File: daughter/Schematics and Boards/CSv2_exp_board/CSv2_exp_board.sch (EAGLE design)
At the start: 139 parts, among them J1 HIROSE-DF40_44-PIN_CONNECTORS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, J2 J-SERIAL-PORT, J3 CORTEX_DEBUG_SMD, J301 HIROSE-DF40_44-PIN_CONNECTORS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, J4 SJ-43514-SMT, J7 J-USB-HIROSE-MICRO-USB, SW1 SPST_TACT-KMR2, SW2 SPST_TACT-KMR2, U1 LOADSWITCH-MIC94164, U10 LOADSWITCH-MIC94164, U11 BMI160, U12 TLV320DAC26IRHB, U13 ADG839YKSZ-500RL7KS_6_ADI-L, U14 LOADSWITCH-MIC94164, U15 LP2980AIM5-2.5/NOPBMF05A_TEX-L, U16 NCP553SQ18T1GSC-82AB_ONS-L, U2 ADA4841-1YRJZ-R7, U205 MPL3115A2, U3 Value, U4 RFM69HCW, U5 Value, U6 Value, U7 LOADSWITCH-MIC94164, U8 LOADSWITCH-MIC94164, U9 LOADSWITCH-MIC94164, X1 32.768kHz, X2 32.768, X3 uFL, X4 uFL, X5 uFL, X6 uFL

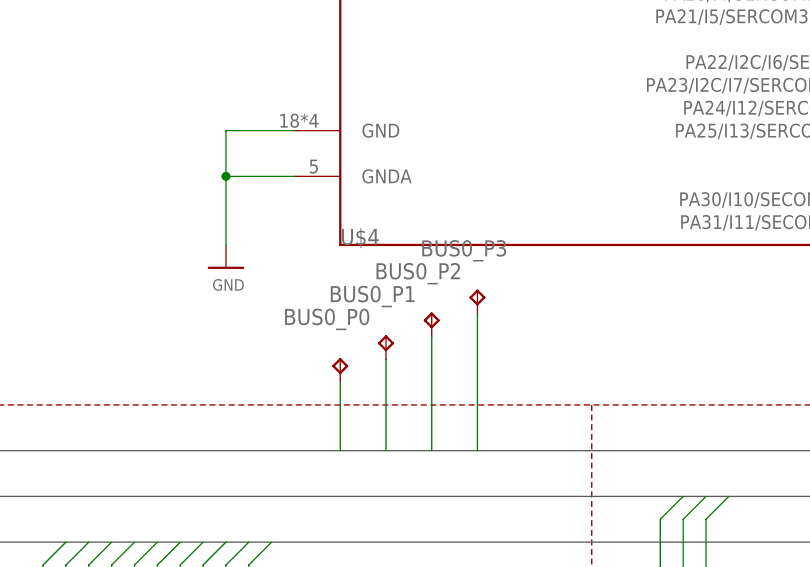
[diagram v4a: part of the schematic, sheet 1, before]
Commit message: DTR-drc resolved, schematic check, routing  check
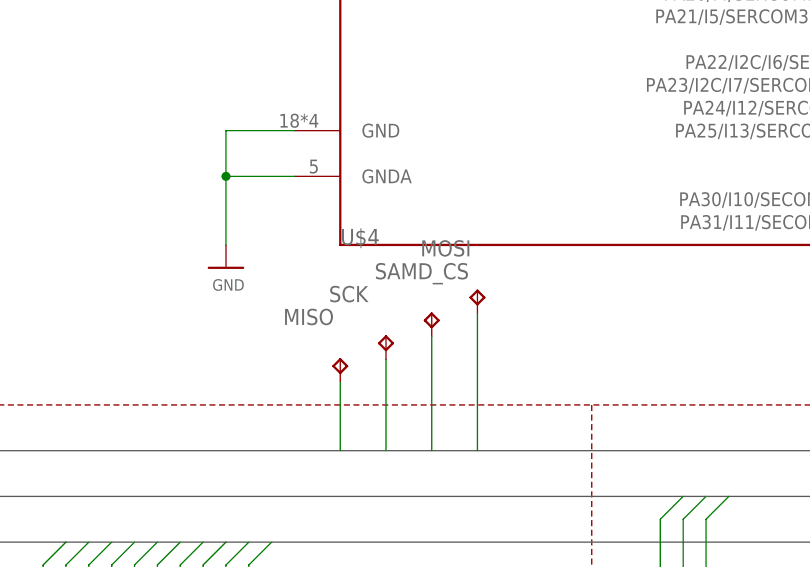
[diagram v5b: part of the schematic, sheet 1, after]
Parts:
- added CODEC_CS: TPTP10SQ, TestPoints:TPTP10SQ
- renumbered BUS0_P0 to MISO, BUS0_P1 to SCK, BUS0_P2 to SAMD_CS, BUS0_P3 to MOSI
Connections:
- net BUS0_GPIO1: now also CODEC_CS.TP
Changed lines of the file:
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@@
 <part name="BUS1_SDA" library="TestPoints" deviceset="TP" device="TP10SQ" package3d_urn="urn:adsk.eagle:package:27962/1" value="TPTP10SQ"/>
 <part name="USB_V" library="TestPoints" deviceset="TP" device="TP10SQ" package3d_urn="urn:adsk.eagle:package:27962/1" value="TPTP10SQ"/>
-<part name="BUS0_P0" library="TestPoints" deviceset="TP" device="TP10SQ" package3d_urn="urn:adsk.eagle:package:27962/1" value="TPTP10SQ"/>
-<part name="BUS0_P1" library="TestPoints" deviceset="TP" device="TP10SQ" package3d_urn="urn:adsk.eagle:package:27962/1" value="TPTP10SQ"/>
-<part name="BUS0_P2" library="TestPoints" deviceset="TP" device="TP10SQ" package3d_urn="urn:adsk.eagle:package:27962/1" value="TPTP10SQ"/>
-<part name="BUS0_P3" library="TestPoints" deviceset="TP" device="TP10SQ" package3d_urn="urn:adsk.eagle:package:27962/1" value="TPTP10SQ"/>
+<part name="MISO" library="TestPoints" deviceset="TP" device="TP10SQ" package3d_urn="urn:adsk.eagle:package:27962/1" value="TPTP10SQ"/>
+<part name="SCK" library="TestPoints" deviceset="TP" device="TP10SQ" package3d_urn="urn:adsk.eagle:package:27962/1" value="TPTP10SQ"/>
+<part name="SAMD_CS" library="TestPoints" deviceset="TP" device="TP10SQ" package3d_urn="urn:adsk.eagle:package:27962/1" value="TPTP10SQ"/>
+<part name="MOSI" library="TestPoints" deviceset="TP" device="TP10SQ" package3d_urn="urn:adsk.eagle:package:27962/1" value="TPTP10SQ"/>
 <part name="J2" library="Connectors" deviceset="J-SERIAL-PORT" device=""/>
 <part name="A1" library="CommonSense-DTR-v1" deviceset="ILA09_CHIP_ANTENNA" device=""/>
@@
 <part name="EN_MEAS" library="TestPoints" deviceset="TP" device="TP10SQ" package3d_urn="urn:adsk.eagle:package:27962/1"/>
 <part name="JP4" library="Connectors" deviceset="JUMPER-SMT_2_NC_PASTE" device="_NO-SILK" package3d_urn="urn:adsk.eagle:package:39283/1" technology="LG" value="JUMPER-SMT_2_NC_PASTELG_NO-SILK"/>
+<part name="CODEC_CS" library="TestPoints" deviceset="TP" device="TP10SQ" package3d_urn="urn:adsk.eagle:package:27962/1" value="TPTP10SQ"/>
 </parts>
 <sheets>
@@
 <attribute name="TP_SIGNAL_NAME" x="344.17" y="199.39" size="1.778" layer="97"/>
 </instance>
-<instance part="BUS0_P0" gate="G$1" x="205.74" y="132.08" smashed="yes">
+<instance part="MISO" gate="G$1" x="205.74" y="132.08" smashed="yes">
 <attribute name="NAME" x="199.39" y="135.89" size="1.778" layer="95"/>
 <attribute name="TP_SIGNAL_NAME" x="207.01" y="130.81" size="1.778" layer="97"/>
 </instance>
-<instance part="BUS0_P1" gate="G$1" x="210.82" y="134.62" smashed="yes">
+<instance part="SCK" gate="G$1" x="210.82" y="134.62" smashed="yes">
 <attribute name="NAME" x="204.47" y="138.43" size="1.778" layer="95"/>
 <attribute name="TP_SIGNAL_NAME" x="212.09" y="133.35" size="1.778" layer="97"/>
 </instance>
-<instance part="BUS0_P2" gate="G$1" x="215.9" y="137.16" smashed="yes">
+<instance part="SAMD_CS" gate="G$1" x="215.9" y="137.16" smashed="yes">
 <attribute name="NAME" x="209.55" y="140.97" size="1.778" layer="95"/>
 <attribute name="TP_SIGNAL_NAME" x="217.17" y="135.89" size="1.778" layer="97"/>
 </instance>
-<instance part="BUS0_P3" gate="G$1" x="220.98" y="139.7" smashed="yes">
+<instance part="MOSI" gate="G$1" x="220.98" y="139.7" smashed="yes">
 <attribute name="NAME" x="214.63" y="143.51" size="1.778" layer="95"/>
 <attribute name="TP_SIGNAL_NAME" x="222.25" y="138.43" size="1.778" layer="97"/>
@@
 </segment>
 </bus>
+<bus name="DTR_BUS1:BUS1_AIN0,BUS1_AIN1,BUS1_GPIO0,BUS1_GPIO1,BUS1_SERCOM_P0,BUS1_SERCOM_P1,BUS1_SERCOM_P2,BUS1_SERCOM_P3">
+<segment>
+<wire x1="7.62" y1="116.84" x2="342.9" y2="116.84" width="0.762" layer="92"/>
+<label x="8.382" y="117.856" size="1.778" layer="95"/>
+</segment>
+</bus>
+<bus name="CTL_BUS:EN_BARO,EN_CODEC,EN_IMU,EN_MEAS,EN_MIC,EN_RADIO,MEAS_BARO,MEAS_CODEC,MEAS_IMU,MEAS_MIC,MEAS_RFM,MEAS_SAMD">
+<segment>
+<wire x1="91.44" y1="111.76" x2="381" y2="111.76" width="0.762" layer="92"/>
+<label x="369.824" y="113.03" size="1.778" layer="95"/>
+</segment>
+</bus>
 <bus name="DTR_BUS0:BUS0_AIN0,BUS0_AIN1,BUS0_GPIO0,BUS0_GPIO1,BUS0_SERCOM_P0,BUS0_SERCOM_P1,BUS0_SERCOM_P2,BUS0_SERCOM_P3">
 <segment>
@@
 <label x="300.99" y="123.444" size="1.778" layer="95"/>
 <wire x1="314.96" y1="121.92" x2="7.62" y2="121.92" width="0.762" layer="92"/>
-</segment>
-</bus>
-<bus name="DTR_BUS1:BUS1_AIN0,BUS1_AIN1,BUS1_GPIO0,BUS1_GPIO1,BUS1_SERCOM_P0,BUS1_SERCOM_P1,BUS1_SERCOM_P2,BUS1_SERCOM_P3">
-<segment>
-<wire x1="7.62" y1="116.84" x2="342.9" y2="116.84" width="0.762" layer="92"/>
-<label x="8.382" y="117.856" size="1.778" layer="95"/>
-</segment>
-</bus>
-<bus name="CTL_BUS:EN_BARO,EN_CODEC,EN_IMU,EN_MEAS,EN_MIC,EN_RADIO,MEAS_BARO,MEAS_CODEC,MEAS_IMU,MEAS_MIC,MEAS_RFM,MEAS_SAMD">
-<segment>
-<wire x1="91.44" y1="111.76" x2="381" y2="111.76" width="0.762" layer="92"/>
-<label x="369.824" y="113.03" size="1.778" layer="95"/>
 </segment>
 </bus>
@@
 </segment>
 <segment>
-<pinref part="BUS0_P0" gate="G$1" pin="TP"/>
+<pinref part="MISO" gate="G$1" pin="TP"/>
 <wire x1="205.74" y1="129.54" x2="205.74" y2="121.92" width="0.1524" layer="91"/>
 </segment>
@@
 </segment>
 <segment>
-<pinref part="BUS0_P3" gate="G$1" pin="TP"/>
+<pinref part="MOSI" gate="G$1" pin="TP"/>
 <wire x1="220.98" y1="137.16" x2="220.98" y2="121.92" width="0.1524" layer="91"/>
 </segment>
@@
 </segment>
 <segment>
-<pinref part="BUS0_P1" gate="G$1" pin="TP"/>
+<pinref part="SCK" gate="G$1" pin="TP"/>
 <wire x1="210.82" y1="132.08" x2="210.82" y2="121.92" width="0.1524" layer="91"/>
 </segment>
@@
 </segment>
 <segment>
-<pinref part="BUS0_P2" gate="G$1" pin="TP"/>
+<pinref part="SAMD_CS" gate="G$1" pin="TP"/>
 <wire x1="215.9" y1="134.62" x2="215.9" y2="121.92" width="0.1524" layer="91"/>
 </segment>
@@
 <attribute name="NAME" x="180.34" y="256.54" size="1.778" layer="95" font="vector" align="bottom-center"/>
 </instance>
+<instance part="CODEC_CS" gate="G$1" x="104.14" y="78.74" smashed="yes">
+<attribute name="NAME" x="102.87" y="80.01" size="1.778" layer="95"/>
+<attribute name="TP_SIGNAL_NAME" x="105.41" y="77.47" size="1.778" layer="97"/>
+</instance>
 </instances>
 <busses>
@@
 <wire x1="55.88" y1="71.12" x2="58.42" y2="73.66" width="0.1524" layer="91"/>
 </segment>
-</net>
+<segment>
+<pinref part="CODEC_CS" gate="G$1" pin="TP"/>
+<wire x1="104.14" y1="76.2" x2="104.14" y2="73.66" width="0.1524" layer="91"/>
+</segment>
+</net>

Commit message: DTR-filled in device specs and double checked the footprint consistency
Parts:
- added C40: 10u, Capacitors:C-0603
- added C43, C44, C45: 0.1u, Capacitors:C-0402
- A1: MPN (none) -> ILA.09; PARTNO (none) -> ILA.09
- AINT, ASCL, ASDA, CS1, CS2, D_IN, D_OUT, EN, MISO, MOSI, R12, RESET, SCK, SCL, SDA, T1, T10, T11, T2, T3, T4, T5, T6, T7, T8, T9, USBV: PARTNO (none) -> *
- ATTINY-817: PARTNO (none) -> ATTINY817MFR
- C1, C14: value 1uF -> 1u; MPN (none) -> C0402C105M8PACTU; PARTNO (none) -> C0402C105M8PACTU; TC (none) -> X5R; TOL (none) -> 20%; VOLTAGE (none) -> 10V
- C10, C17, C19, C21, C23, C29: MANUFACTURER (none) -> Yageo; MPN (none) -> CC0402KRX5R5BB105; TC (none) -> X5R
- C11, C18, C20, C22, C24, C30: value 100n -> 0.1u; MANUFACTURER (none) -> Yageo; MPN (none) -> CC0402KRX5R5BB104; TC (none) -> X5R
- C12: value 4.7nF -> 4.7u; device Capacitors:C-0402 -> Capacitors:C-0603; MPN (none) -> C0603C475K8PACTU; PARTNO CC0402KRX5R5BB105 -> C0603C475K8PACTU; TC (none) -> X5R; VOLTAGE (none) -> 10V
- C13: value 100nF -> 0.1u; MPN (none) -> C0402C104K4RACTU; PARTNO CC0402KRX5R5BB105 -> C0402C104K4RACTU; VOLTAGE (none) -> 16V
- C15, C16, JP14, JP16, SJ1, SJ2, X1: BOM (none) -> EXCLUDE; PARTNO (none) -> *
- C2: value 22pF -> 5.5p; MPN (none) -> CBR04C559B5GAC; PARTNO (none) -> CBR04C559B5GAC; TC (none) -> C0G, NP0; TOL (none) -> 0.1p; VOLTAGE (none) -> 50V
- C203, C204, C25: value 0.1uF -> 0.1u; MPN (none) -> C0402C104K4RACTU; PARTNO (none) -> C0402C104K4RACTU; VOLTAGE (none) -> 16V
- C26: value (none) -> 22p; MPN (none) -> CBR04C220F5GAC; PARTNO (none) -> CBR04C220F5GAC; TOL (none) -> 1%; VOLTAGE (none) -> 50V
- C3: MANUFACTURER (none) -> Murata; MPN (none) -> GJM1555C1H3R9WB01D; PARTNO (none) -> GJM1555C1H3R9WB01D; TOL (none) -> 0.05p; VOLTAGE (none) -> 50V
- C31, C32: value (none) -> 47u; device Capacitors:C-0402 -> Capacitors:C-0603; MANUFACTURER (none) -> AVX; MPN (none) -> 06036D476MAT2A; PARTNO (none) -> 06036D476MAT2A; TC (none) -> X5R; TOL (none) -> 20%
- C33: value (none) -> 0.1u; MANUFACTURER (none) -> Murata; MPN (none) -> GRM155R71E104KE14J; PARTNO (none) -> GRM155R71E104KE14J; VOLTAGE (none) -> 25V
- C34, C38: MANUFACTURER (none) -> Murata; MPN (none) -> GRM155R71E104KE14J; PARTNO (none) -> GRM155R71E104KE14J; VOLTAGE (none) -> 25V
- C35, C39: MANUFACTURER (none) -> Murata; MPN (none) -> GRM188R60J106KE47D; PARTNO (none) -> GRM188R60J106KE47D; TC (none) -> X5R
- C36: MANUFACTURER (none) -> TDK; MPN (none) -> C1005X7R1C104K050BC; PARTNO (none) -> C1005X7R1C104K050BC; VOLTAGE (none) -> 16V
- C37: ESR (none) -> 7.5; MANUFACTURER (none) -> AVX; MPN (none) -> TACL106K010XTA; PARTNO (none) -> TACL106K010XTA; VOLTAGE (none) -> 10V
- C4: value 22pF -> 5.5p; MPN (none) -> CBR04C559B5GAC; PARTNO (none) -> CBR04C559B5GAC; TC (none) -> C0G,NP0; TOL (none) -> 0.1p; VOLTAGE (none) -> 50V
- C41: ESR (none) -> 15; MANUFACTURER (none) -> AVX; PARTNO (none) -> TACK225M006QTA; TOL (none) -> 20%
- C42: value 2.2u -> 1u; MANUFACTURER (none) -> TDK; MPN (none) -> C1005X7S1A105K050BC; PARTNO (none) -> C1005X7S1A105K050BC; TC (none) -> X7S; VOLTAGE (none) -> 10V
- C46: MPN (none) -> C0402C472K3RACTU; PARTNO (none) -> C0402C472K3RACTU; VOLTAGE (none) -> 25V
- C5: MANUFACTURER (none) -> Murata; MPN (none) -> GJM1555C1H2R2WB01D; PARTNO (none) -> GJM1555C1H2R2WB01D; TOL (none) -> 0.05p; VOLTAGE (none) -> 50V
- C6: value 4.7u -> 0.68u; MANUFACTURER (none) -> Yageo; MPN (none) -> CC0402KRX5R5BB684; PARTNO (none) -> CC0402KRX5R5BB684; TC (none) -> X5R
- C7: MPN (none) -> C0402C104K4RACTU; PARTNO (none) -> C0402C104K4RACTU; VOLTAGE (none) -> 16V
- C8: MPN (none) -> C0402C105M8PACTU; PARTNO (none) -> C0402C105M8PACTU; TC (none) -> X5R; VOLTAGE (none) -> 10V
- C9: value 10uF -> 10u; device Capacitors:C-0402 -> Capacitors:C-0603; MANUFACTURER (none) -> Murata; MPN (none) -> GRM188R60J106KE47D; PARTNO (none) -> GRM188R60J106KE47D; TC (none) -> X5R
- J-TAG/UPDI: value ATTINY_AVR_DEBUG_SMD -> ATTINY_AVR_DEBUG; device CommonSense-DTR-v1:ATTINY_AVR_DEBUG_SMD -> CommonSense-DTR-v1:ATTINY_AVR_DEBUG; MPN (none) -> FTSH-105-01-L-DV-K; PARTNO (none) -> FTSH-105-01-L-DV-K; SPICEPREFIX X -> (none)
- J1, J301: MPN (none) -> DF40HC(3.0)-44DS-0.4V(51); PARTNO (none) -> *; PART_NO DF40HC(3.0)-44DS-0.4V(51) -> (none)
- J2: PARTNO (none) -> PH1-06-UA
- J3: MPN (none) -> FTSH-105-01-L-DV-K; PARTNO (none) -> FTSH-105-01-L-DV-K
- J4: MPN (none) -> SJ-43514-SMT; PARTNO (none) -> *
- J7: PARTNO (none) -> ZX62D-AB-5P8(30)
- L1: value L0402 -> 1.2n; MPN (none) -> LQP15MN1N2W02D; PARTNO (none) -> LQP15MN1N2W02D
- MK1: device SPW2430HR5H-B:SPW2430HR5H-B -> CommonSense-DTR-v1:SPW2430HR5H-B; MPN (none) -> SPW2430HR5H-B; PARTNO (none) -> SPW2430HR5H-B
- R1: value 1.5k -> 4.99k; MPN (none) -> ERA-2AEB4991X; OC_NEWARK unknown -> (none); PARTNO (none) -> ERA-2AEB4991X; TOL (none) -> 0.1%
- R10: MPN (none) -> ERJ-2RKF1003X; PARTNO (none) -> ERJ-2RKF1003X; TOL (none) -> 1%
- R11: MPN (none) -> ERJ-2GEJ104X; PARTNO (none) -> ERJ-2GEJ104X
- R2: value 100k -> 82.5k; MF BOURNS -> (none); MPN 3549S-1AA-102A -> ERA-2AEB8252X; OC_NEWARK 17M3640 -> (none); PARTNO (none) -> ERA-2AEB8252X; TOL (none) -> 0.1%
- R27, R28: value (none) -> 0; MANUFACTURER (none) -> Stackpole; MPN (none) -> RMCF0402ZT0R00; PARTNO (none) -> RMCF0402ZT0R00; TOL (none) -> Jumper
- R3, R4: value 10k -> 100k; MANUFACTURER (none) -> Yageo; MPN (none) -> RT0402BRD07100KL; OC_NEWARK unknown -> (none); PARTNO (none) -> RT0402BRD07100KL; TOL (none) -> 0.1%
- R5, R6: MPN (none) -> ERJ2RKF4701X; PARTNO (none) -> ERJ2RKF4701X; TOL (none) -> 1%
- R7: value (none) -> 50; device Resistors:R-0402 -> Resistors:R-0805; MANUFACTURER (none) -> Vishay; PARTNO (none) -> Y402250R0000A9R; TOL (none) -> 0.05%
- R8: value (none) -> 2.2k; device Resistors:R-0402 -> Resistors:R-0603; MPN (none) -> ERJ-3GEYJ222V; PARTNO (none) -> ERJ-3GEYJ222V
- R9: MPN (none) -> ERJ-2RKF39R0X; PARTNO (none) -> ERJ-2RKF39R0X; TOL (none) -> 1%
- R_SENSE: MANUFACTURER (none) -> Vishay Dale; MPN (none) -> CRCW04021R33FKED; PARTNO CRCW06031R33FKEA -> CRCW04021R33FKED; TOL (none) -> 1%
- SJ3: BOM (none) -> EXCLUDE
- SW1, SW2: device adafruit:SPST_TACT-KMR2 -> CommonSense-DTR-v1:SPST_TACT-KMR2; MPN (none) -> KMR241NG ULC LFS; PARTNO (none) -> KMR241NG ULC LFS
- U$4: MPN (none) -> ATSAMD21G18A-MFT; PARTNO (none) -> ATSAMD21G18A-MFT
- U1, U10, U14, U7, U8, U9: PARTNO (none) -> MIC94164YCS-TR
- U11: MPN (none) -> BMI160; PARTNO (none) -> BMI160
- U12: PARTNO (none) -> TLV320DAC26IRHB
- U13: MPN (none) -> ADG839YKSZ-500RL7; PARTNO (none) -> ADG839YKSZ-500RL7
- U15: MANUFACTURER_PART_NUMBER (none) -> LP2980AIM5-3.0/NOPB; PARTNO (none) -> LP2980AIM5-3.0/NOPB
- U16: MPN (none) -> NCP553SQ18T1G; PARTNO (none) -> NCP553SQ18T1G
- U2: value ADA4841-1YRJZ-R7 -> ADA4841-1YRJZ-R7RJ_6-L; device ADA1484:ADA4841-1YRJZ-R7 -> CommonSense-DTR-v1:ADA4841-1YRJZ-R7RJ_6-L; MPN (none) -> ADA48411YRJZR7; OC_NEWARK unknown -> (none); PARTNO (none) -> ADA48411YRJZR7
- U205: PARTNO (none) -> MPL-3115A2
- U3, U5, U6: MPN (none) -> TS3A24159DGSR; PARTNO (none) -> TS3A24159DGSR
- U4: MPN (none) -> RFM95CW; PARTNO (none) -> *
- X2: LOAD_CAPACITY (none) -> 6p; MANUFACTURER (none) -> NDK; MPN (none) -> NX3215SA-32.768K-STD-MUA-14; PARTNO (none) -> NX3215SA-32.768K-STD-MUA-14; TOL (none) -> 20ppm
- X3, X4, X5, X6: MPN (none) -> U.FL-R-SMT-1(01); PARTNO (none) -> U.FL-R-SMT-1(01)
- renumbered ATT_INT to AINT, ATT_SCL to ASCL, ATT_SDA to ASDA, BUS1_SCL to SCL, BUS1_SDA to SDA, C27 to R27, C28 to R28, C3-4.7N to C46, CODEC_CS to CS2, DETECT_IN to D_IN, DETECT_OUT to D_OUT, EN_BARO to T7, EN_CODEC to T2, EN_IMU to T8, EN_MEAS to EN, EN_MIC to T3, EN_RADIO to T11, MEAS_BARO to T5, MEAS_CODEC to T1, MEAS_IMU to T6, MEAS_MIC to T4, MEAS_RFM to T9, MEAS_SAMD to T10, R1-100K to R10, R3-39R to R9, SAMD_CS to CS1, TP1 to RESET, USB_V to USBV
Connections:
- net +3V3_BARO: now also C40.2
- net +3V3_DTR: now also C43.1, C44.1, C45.1
- net GND: now also C40.1, C43.2, C44.2, C45.2, J3.GNDDTCT
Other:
- moved on the sheet: C13, C37, C9, J-TAG/UPDI

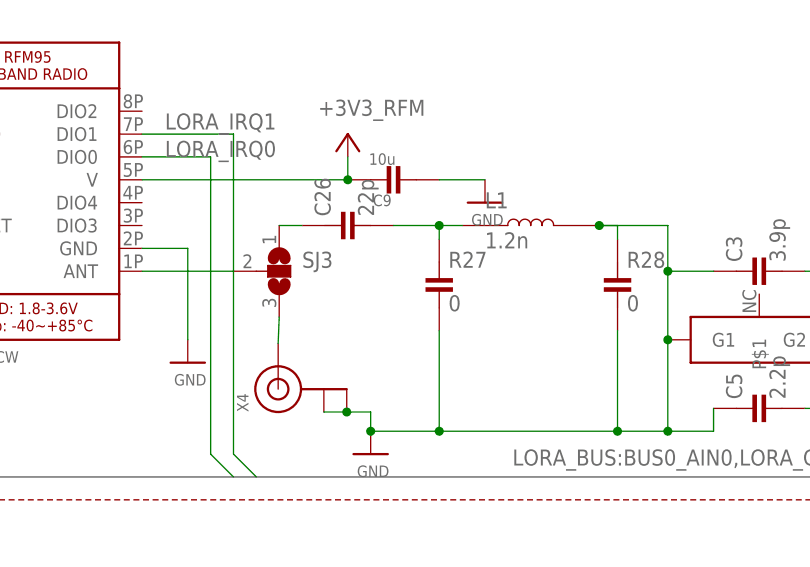
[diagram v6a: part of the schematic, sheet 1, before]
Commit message: DTR-rounded corners, generated BOM
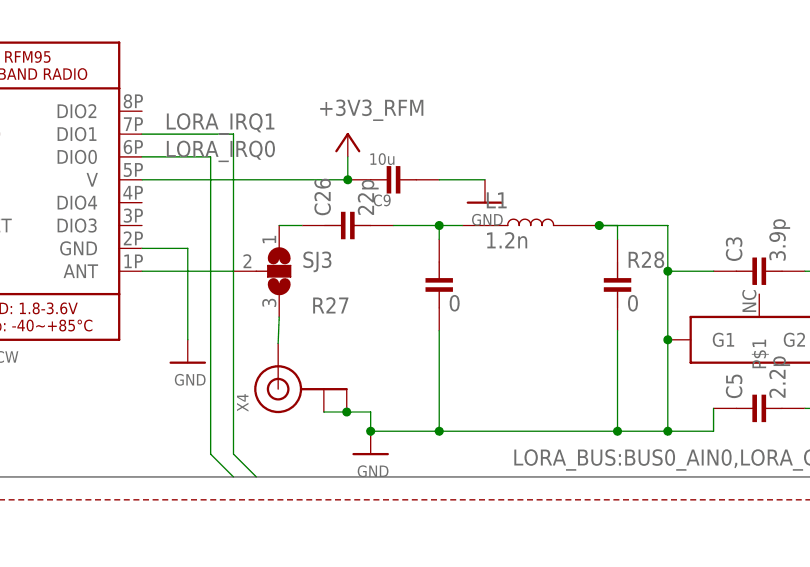
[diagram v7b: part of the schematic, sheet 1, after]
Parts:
- C25: device Capacitors:C-0603 -> Capacitors:C-0402
- J1: PARTNO * -> DF40HC(3.0)-44DS-0.4V(51)
- J301: MPN DF40HC(3.0)-44DS-0.4V(51) -> DF40C-44DP-0.4V(51); PARTNO * -> DF40C-44DP-0.4V(51)
- J4: PARTNO * -> SJ-43514-SMT
- R11: MPN ERJ-2GEJ104X -> ERJ-2RKF1003X; PARTNO ERJ-2GEJ104X -> ERJ-2RKF1003X; TOL (none) -> 1%
- R12: device Resistors:R-0402 -> Resistors:R-1210; PARTNO * -> ERJ-14Y0R00U; TOL (none) -> Jumper
- RESET: BOM (none) -> EXCLUDE
- U4: PARTNO * -> RFM95W
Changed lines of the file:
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@@
 <part name="U4" library="Radios" deviceset="RFM95" device="C" value="RFM69HCW">
 <attribute name="MPN" value="RFM95CW"/>
-<attribute name="PARTNO" value="*"/>
+<attribute name="PARTNO" value="RFM95W"/>
 </part>
 <part name="U$17" library="Supplies" deviceset="GND" device=""/>
@@
 <part name="GND1" library="Supplies" deviceset="GND" device=""/>
 <part name="J301" library="Connectors" deviceset="HIROSE-DF40_44-PIN_CONNECTORS" device="-HEADER" value="HIROSE-DF40_44-PIN_CONNECTORS-HEADER">
-<attribute name="MPN" value="DF40HC(3.0)-44DS-0.4V(51)"/>
-<attribute name="PARTNO" value="*"/>
+<attribute name="MPN" value="DF40C-44DP-0.4V(51)"/>
+<attribute name="PARTNO" value="DF40C-44DP-0.4V(51)"/>
 </part>
 <part name="GND22" library="Supplies" deviceset="GND" device=""/>
 <part name="J1" library="Connectors" deviceset="HIROSE-DF40_44-PIN_CONNECTORS" device="-RECEPTACLE">
 <attribute name="MPN" value="DF40HC(3.0)-44DS-0.4V(51)"/>
-<attribute name="PARTNO" value="*"/>
+<attribute name="PARTNO" value="DF40HC(3.0)-44DS-0.4V(51)"/>
 </part>
 <part name="GND4" library="Supplies" deviceset="GND" device=""/>
@@
 <part name="+3V21" library="Supplies" deviceset="+3V3" device=""/>
 <part name="GND24" library="Supplies" deviceset="GND" device=""/>
-<part name="C25" library="Capacitors" deviceset="C-" device="0603" value="0.1u">
+<part name="C25" library="Capacitors" deviceset="C-" device="0402" value="0.1u">
 <attribute name="MPN" value="C0402C104K4RACTU"/>
 <attribute name="PARTNO" value="C0402C104K4RACTU"/>
@@
 <part name="J4" library="CommonSense-DTR-v1" deviceset="SJ-43514-SMT" device="">
 <attribute name="MPN" value="SJ-43514-SMT"/>
-<attribute name="PARTNO" value="*"/>
+<attribute name="PARTNO" value="SJ-43514-SMT"/>
 </part>
 <part name="U13" library="CommonSense-DTR-v1" deviceset="ADG839YKSZ-500RL7" device="KS_6_ADI-L">
@@
 </part>
 <part name="R11" library="Resistors" deviceset="R-" device="0402" value="100k">
-<attribute name="MPN" value="ERJ-2GEJ104X"/>
-<attribute name="PARTNO" value="ERJ-2GEJ104X"/>
+<attribute name="MPN" value="ERJ-2RKF1003X"/>
+<attribute name="PARTNO" value="ERJ-2RKF1003X"/>
+<attribute name="TOL" value="1%"/>
 </part>
 <part name="RESET" library="TestPoints" deviceset="TP" device="TP11SQ" package3d_urn="urn:adsk.eagle:package:27965/1">
+<attribute name="BOM" value="EXCLUDE"/>
 <attribute name="PARTNO" value="*"/>
 </part>
 <part name="GND32" library="Supplies" deviceset="GND" device=""/>
 <part name="GND35" library="Supplies" deviceset="GND" device=""/>
-<part name="R12" library="Resistors" deviceset="R-" device="0402">
-<attribute name="PARTNO" value="*"/>
+<part name="R12" library="Resistors" deviceset="R-" device="1210">
+<attribute name="PARTNO" value="ERJ-14Y0R00U"/>
+<attribute name="TOL" value="Jumper"/>
 </part>
 <part name="U15" library="CommonSense-DTR-v1" deviceset="LP2980AIM5-2.5/NOPB" device="MF05A_TEX-L">
@@
 </instance>
 <instance part="R27" gate="G$1" x="96.52" y="224.536" smashed="yes">
-<attribute name="NAME" x="97.536" y="226.441" size="1.778" layer="95"/>
+<attribute name="NAME" x="82.296" y="221.361" size="1.778" layer="95"/>
 <attribute name="VALUE" x="97.536" y="221.615" size="1.778" layer="96"/>
 <attribute name="MPN" x="96.52" y="224.536" size="1.778" layer="96" display="off"/>
@@
 <attribute name="TP_SIGNAL_NAME" x="176.53" y="49.53" size="1.778" layer="97"/>
 <attribute name="PARTNO" x="175.26" y="50.8" size="1.778" layer="96" display="off"/>
+<attribute name="BOM" x="175.26" y="50.8" size="1.778" layer="96" display="off"/>
 </instance>
 <instance part="GND32" gate="1" x="215.9" y="17.78" smashed="yes"/>
